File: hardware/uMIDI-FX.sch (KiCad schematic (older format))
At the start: 0 parts

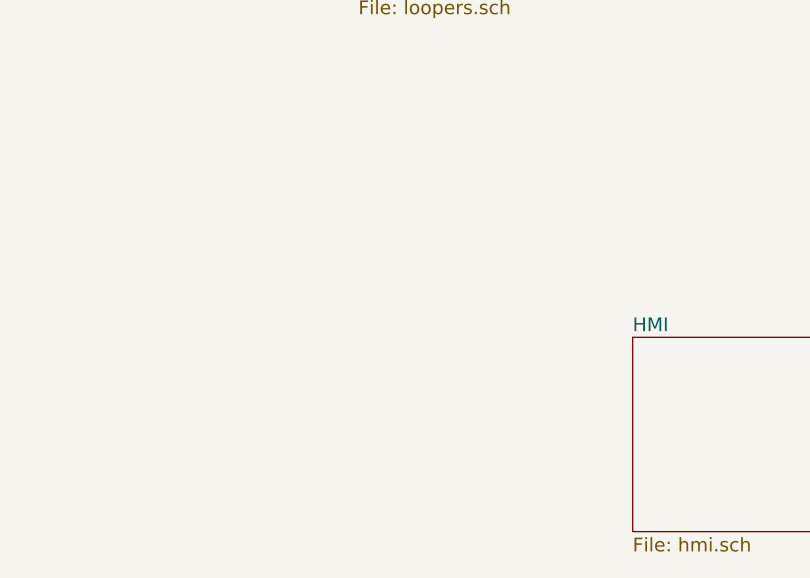
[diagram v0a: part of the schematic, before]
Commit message: Stub port expander subcircuit
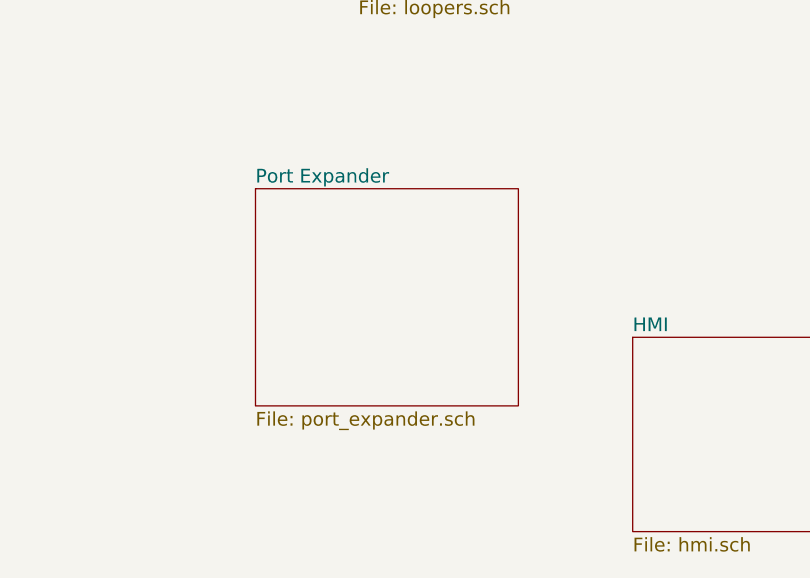
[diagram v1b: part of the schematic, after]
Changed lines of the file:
@@
 LIBS:stacked_jack
 LIBS:relais
+LIBS:tca9555
 LIBS:uMIDI-FX-cache
 EELAYER 24 0
@@
 $Descr A4 11693 8268
 encoding utf-8
-Sheet 1 21
+Sheet 1 22
 Title ""
 Date ""
@@
 F10 "SwitchRing" I L 5150 3250 60
 $EndSheet
+$Sheet
+S 4700 4250 1150 950
+U 54E9D1C8
+F0 "Port Expander" 60
+F1 "port_expander.sch" 60
+$EndSheet
 $EndSCHEMATC

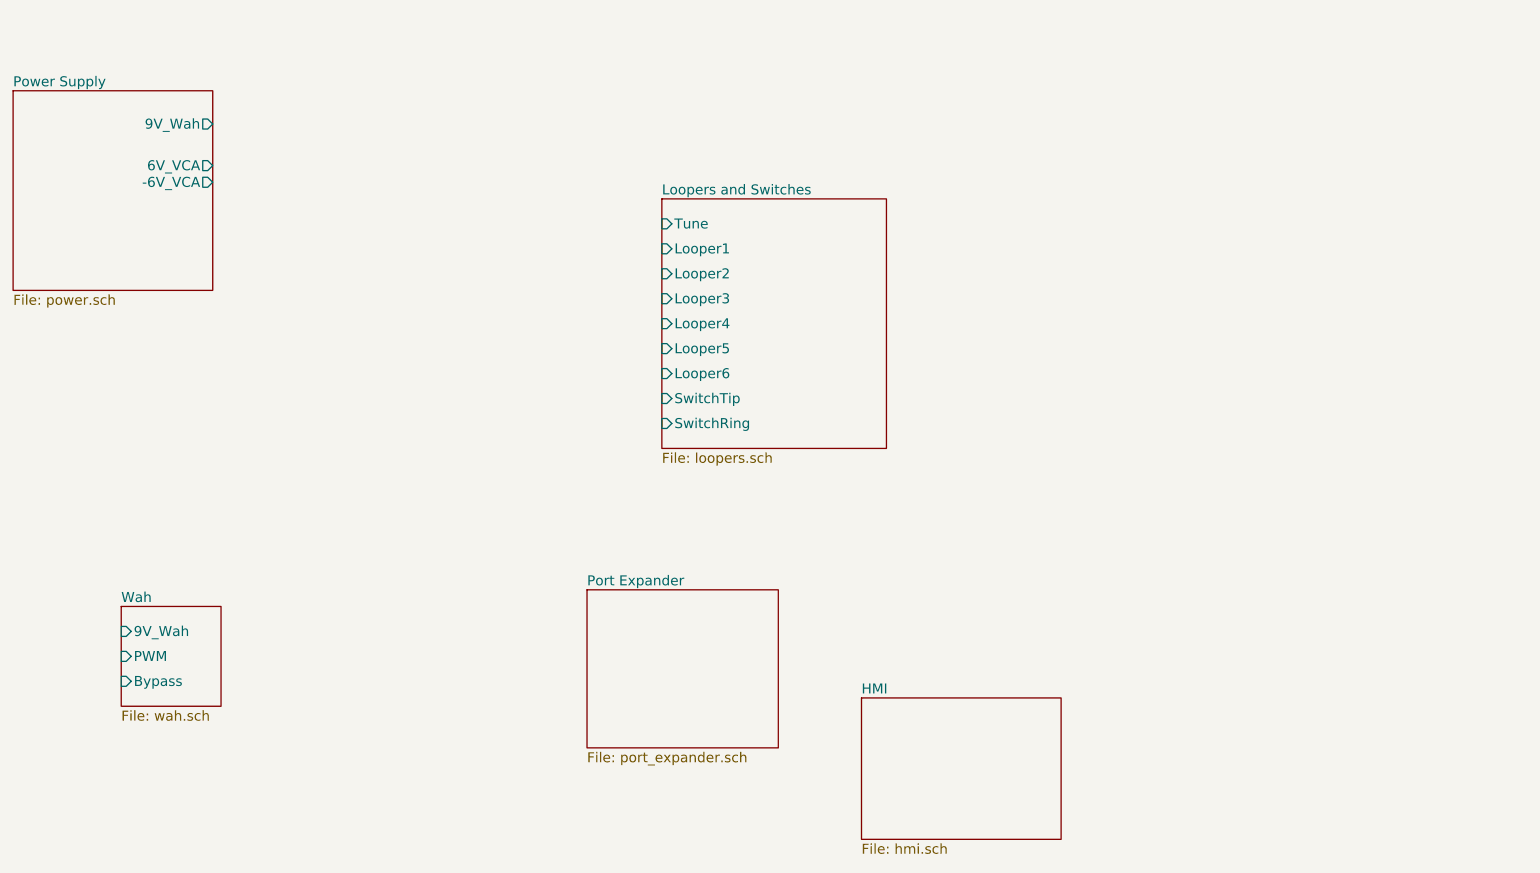
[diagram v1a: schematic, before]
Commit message: Draw port expander and integrate first instance
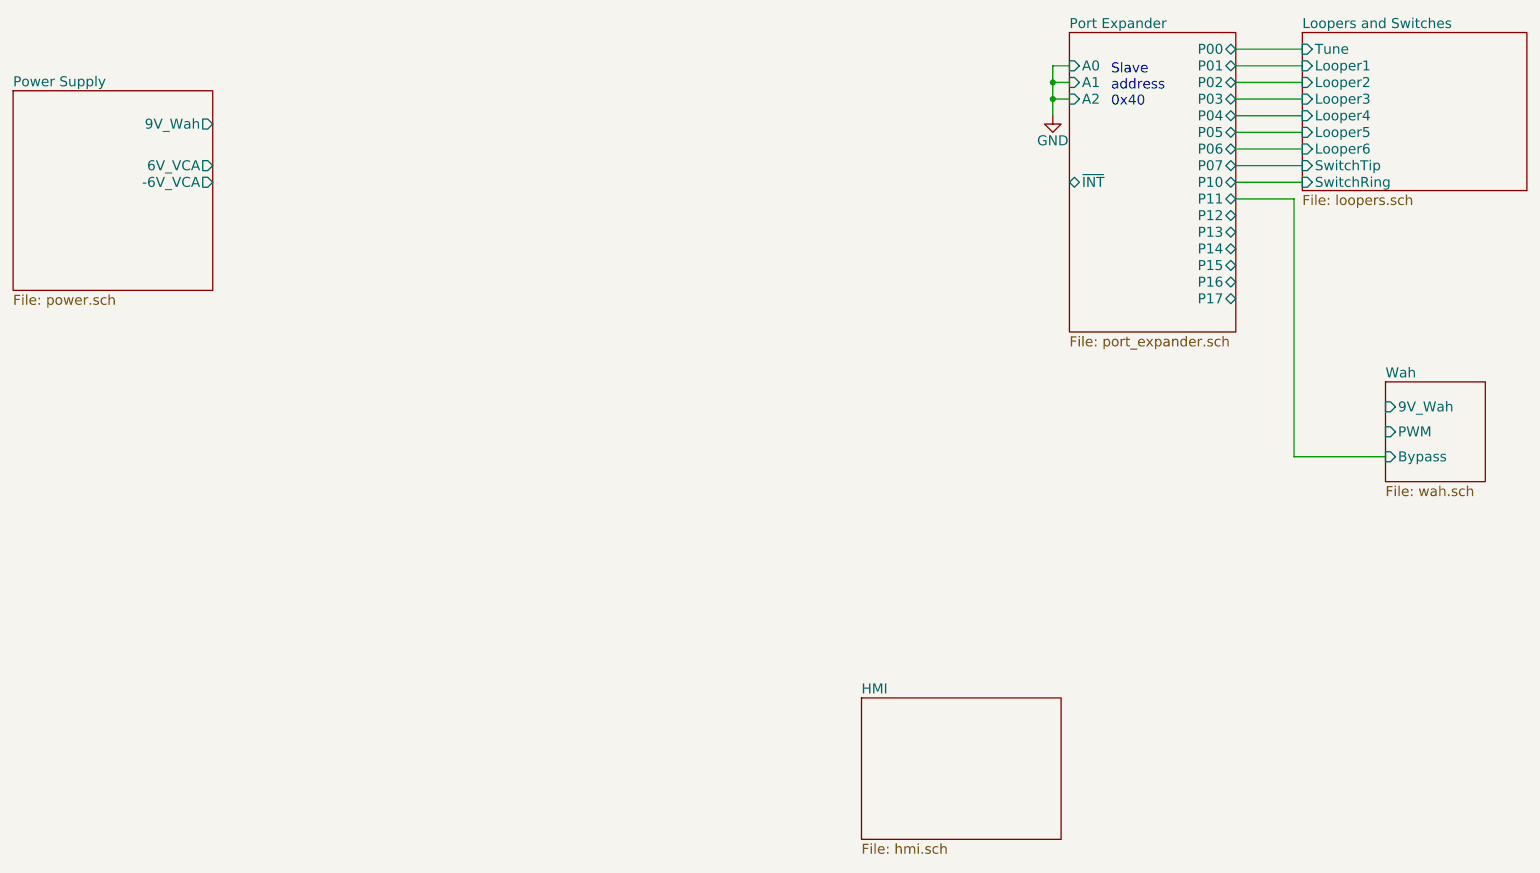
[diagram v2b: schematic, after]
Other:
- note added: "Slave\naddress\n0x40"
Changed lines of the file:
@@
 $EndSheet
 $Sheet
-S 1900 4350 600  600
+S 9500 3000 600  600
 U 54D5349F
 F0 "Wah" 60
 F1 "wah.sch" 60
-F2 "9V_Wah" I L 1900 4500 60
-F3 "PWM" I L 1900 4650 60
-F4 "Bypass" I L 1900 4800 60
+F2 "9V_Wah" I L 9500 3150 60
+F3 "PWM" I L 9500 3300 60
+F4 "Bypass" I L 9500 3450 60
 $EndSheet
 $Sheet
-S 5150 1900 1350 1500
+S 9000 900  1350 950
 U 54D120FF
 F0 "Loopers and Switches" 60
 F1 "loopers.sch" 60
-F2 "Tune" I L 5150 2050 60
-F3 "Looper1" I L 5150 2200 60
-F4 "Looper2" I L 5150 2350 60
-F5 "Looper3" I L 5150 2500 60
-F6 "Looper4" I L 5150 2650 60
-F7 "Looper5" I L 5150 2800 60
-F8 "Looper6" I L 5150 2950 60
-F9 "SwitchTip" I L 5150 3100 60
-F10 "SwitchRing" I L 5150 3250 60
+F2 "Tune" I L 9000 1000 60
+F3 "Looper1" I L 9000 1100 60
+F4 "Looper2" I L 9000 1200 60
+F5 "Looper3" I L 9000 1300 60
+F6 "Looper4" I L 9000 1400 60
+F7 "Looper5" I L 9000 1500 60
+F8 "Looper6" I L 9000 1600 60
+F9 "SwitchTip" I L 9000 1700 60
+F10 "SwitchRing" I L 9000 1800 60
 $EndSheet
 $Sheet
-S 4700 4250 1150 950
+S 7600 900  1000 1800
 U 54E9D1C8
 F0 "Port Expander" 60
 F1 "port_expander.sch" 60
+F2 "P00" B R 8600 1000 60
+F3 "P01" B R 8600 1100 60
+F4 "P02" B R 8600 1200 60
+F5 "P03" B R 8600 1300 60
+F6 "P04" B R 8600 1400 60
+F7 "P05" B R 8600 1500 60
+F8 "P06" B R 8600 1600 60
+F9 "P07" B R 8600 1700 60
+F10 "P10" B R 8600 1800 60
+F11 "P11" B R 8600 1900 60
+F12 "P12" B R 8600 2000 60
+F13 "P13" B R 8600 2100 60
+F14 "P14" B R 8600 2200 60
+F15 "P15" B R 8600 2300 60
+F16 "P16" B R 8600 2400 60
+F17 "P17" B R 8600 2500 60
+F18 "A0" I L 7600 1100 60
+F19 "A1" I L 7600 1200 60
+F20 "A2" I L 7600 1300 60
+F21 "~INT" T L 7600 1800 60
 $EndSheet
+Wire Wire Line
+	8600 1000 9000 1000
+Wire Wire Line
+	8600 1100 9000 1100
+Wire Wire Line
+	8600 1200 9000 1200
+Wire Wire Line
+	8600 1300 9000 1300
+Wire Wire Line
+	8600 1400 9000 1400
+Wire Wire Line
+	8600 1500 9000 1500
+Wire Wire Line
+	8600 1600 9000 1600
+Wire Wire Line
+	8600 1700 9000 1700
+Wire Wire Line
+	8600 1800 9000 1800
+Wire Wire Line
+	9500 3450 8950 3450
+Wire Wire Line
+	8950 3450 8950 1900
+Wire Wire Line
+	8950 1900 8600 1900
+$Comp
+L GND #PWR?
+U 1 1 54EADD45
+P 7500 1400
+F 0 "#PWR?" H 7500 1150 60  0001 C CNN
+F 1 "GND" H 7500 1250 60  0000 C CNN
+F 2 "" H 7500 1400 60  0000 C CNN
+F 3 "" H 7500 1400 60  0000 C CNN
+	1    7500 1400
+	1    0    0    -1
+$EndComp
+Wire Wire Line
+	7500 1400 7500 1100
+Wire Wire Line
+	7500 1100 7600 1100
+Wire Wire Line
+	7600 1200 7500 1200
+Connection ~ 7500 1200
+Wire Wire Line
+	7600 1300 7500 1300
+Connection ~ 7500 1300
+Text Notes 7850 1350 0    60   ~ 0
+Slave\naddress\n0x40
 $EndSCHEMATC

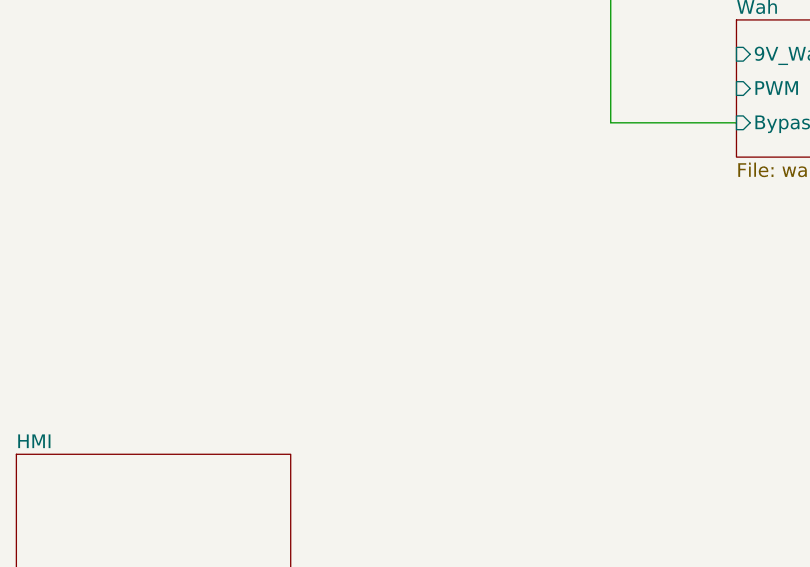
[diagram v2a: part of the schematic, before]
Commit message: Stub VCA schematic sheet
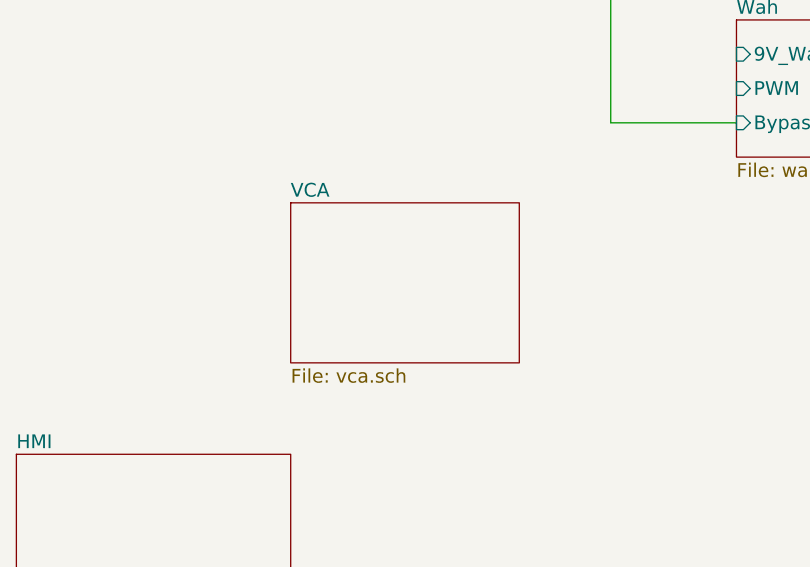
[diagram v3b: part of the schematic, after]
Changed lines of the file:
@@
 $Descr A4 11693 8268
 encoding utf-8
-Sheet 1 22
+Sheet 1 23
 Title ""
 Date ""
@@
 Text Notes 7850 1350 0    60   ~ 0
 Slave\naddress\n0x40
+$Sheet
+S 7550 3800 1000 700
+U 54EA3170
+F0 "VCA" 60
+F1 "vca.sch" 60
+$EndSheet
 $EndSCHEMATC
